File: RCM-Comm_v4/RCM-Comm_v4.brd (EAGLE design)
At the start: 50.8 x 66 mm, 27 parts, among them J1 BLACKFIN_HEADER, J2 2199230-4

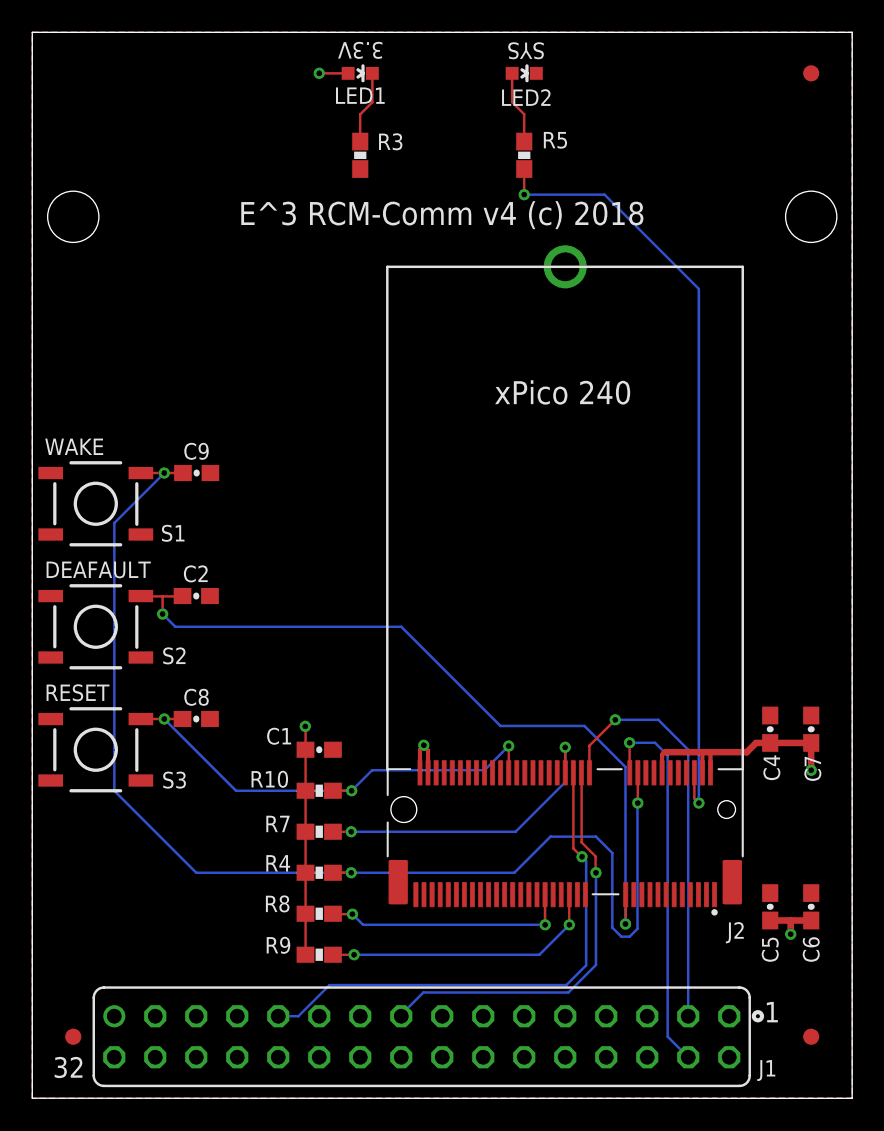
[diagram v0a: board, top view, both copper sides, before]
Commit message: Added DEFAULT ENABLE header back in, re-rendered top and bottom for approval.
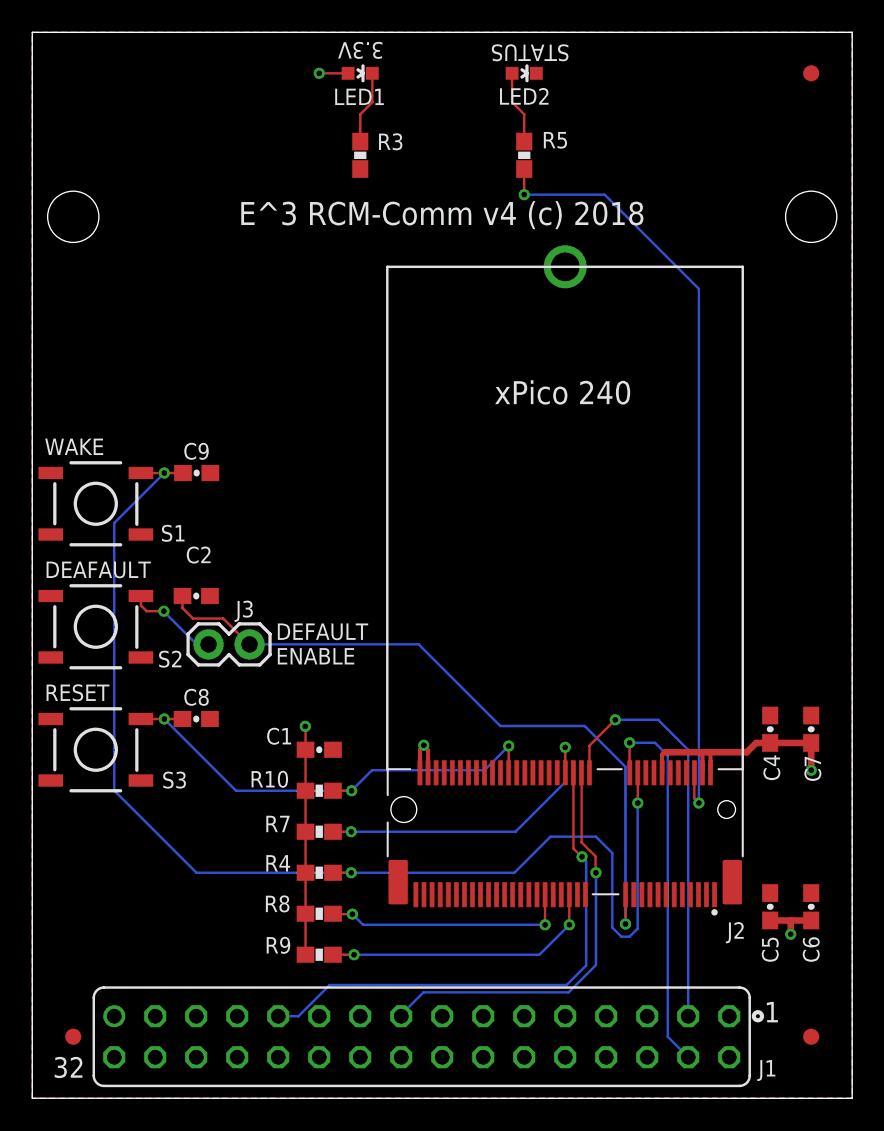
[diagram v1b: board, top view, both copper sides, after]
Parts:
- added J3: (no value), SparkFun-Connectors:1X02
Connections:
- new net N$1: J3.1, S2.3
- net !DEFAULT!: now also J3.2; no longer S2.3
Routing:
- net N$1: track 0.00 -> 5.79 mm, vias 0 -> 1
- net !DEFAULT!: track 47.8 -> 43.9 mm, vias 2 -> 1
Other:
- board text added: "DEFAULT ENABLE"
- board text added: "STATUS"
- board text removed: "SYS"
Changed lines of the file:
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@@
 <layer number="20" name="Dimension" color="15" fill="1" visible="yes" active="yes"/>
 <layer number="21" name="tPlace" color="15" fill="1" visible="yes" active="yes"/>
-<layer number="22" name="bPlace" color="15" fill="1" visible="yes" active="yes"/>
+<layer number="22" name="bPlace" color="15" fill="1" visible="no" active="yes"/>
 <layer number="23" name="tOrigins" color="15" fill="1" visible="yes" active="yes"/>
-<layer number="24" name="bOrigins" color="15" fill="1" visible="yes" active="yes"/>
+<layer number="24" name="bOrigins" color="15" fill="1" visible="no" active="yes"/>
 <layer number="25" name="tNames" color="15" fill="1" visible="yes" active="yes"/>
-<layer number="26" name="bNames" color="15" fill="1" visible="yes" active="yes"/>
+<layer number="26" name="bNames" color="15" fill="1" visible="no" active="yes"/>
 <layer number="27" name="tValues" color="15" fill="1" visible="yes" active="yes"/>
 <layer number="28" name="bValues" color="15" fill="1" visible="yes" active="yes"/>
@@
 <layer number="230" name="230bmp" color="7" fill="1" visible="yes" active="yes"/>
 <layer number="231" name="231bmp" color="7" fill="1" visible="yes" active="yes"/>
+<layer number="232" name="Eagle3D_PG2" color="7" fill="1" visible="yes" active="yes"/>
+<layer number="233" name="Eagle3D_PG3" color="7" fill="1" visible="yes" active="yes"/>
 <layer number="248" name="Housing" color="7" fill="1" visible="yes" active="yes"/>
 <layer number="249" name="Edge" color="7" fill="1" visible="yes" active="yes"/>
@@
 <wire x1="2.54" y1="0" x2="2.54" y2="66.04" width="0" layer="20"/>
 <circle x="47.498" y="5.08" radius="0.254" width="0.254" layer="21"/>
-<text x="15.3162" y="54.102" size="1.4224" layer="21">E^3 RCM-Comm v4 (c) 2018</text>
-<text x="34.3154" y="65.405" size="1.016" layer="21" ratio="10" rot="SR180">SYS</text>
-<text x="24.3332" y="65.4304" size="1.016" layer="21" ratio="10" rot="SR180">3.3V</text>
-<text x="3.302" y="39.8526" size="1.016" layer="21" ratio="10" rot="SR0">WAKE</text>
-<text x="3.302" y="32.2326" size="1.016" layer="21" ratio="10" rot="SR0">DEAFAULT</text>
-<text x="3.302" y="24.6126" size="1.016" layer="21" ratio="10" rot="SR0">RESET</text>
+<text x="15.3162" y="54.102" size="1.4224" layer="21" font="vector">E^3 RCM-Comm v4 (c) 2018</text>
+<text x="35.8394" y="65.278" size="1.016" layer="21" font="vector" ratio="10" rot="SR180">STATUS</text>
+<text x="24.3332" y="65.4304" size="1.016" layer="21" font="vector" ratio="10" rot="SR180">3.3V</text>
+<text x="3.302" y="39.8526" size="1.016" layer="21" font="vector" ratio="10" rot="SR0">WAKE</text>
+<text x="3.302" y="32.2326" size="1.016" layer="21" font="vector" ratio="10" rot="SR0">DEAFAULT</text>
+<text x="3.302" y="24.6126" size="1.016" layer="21" font="vector" ratio="10" rot="SR0">RESET</text>
 <text x="49.0982" y="37.8968" size="1.4224" layer="22" rot="MR0">  Engineering^3, 2018
 http://engineering3.org</text>
@@
 <wire x1="24.5364" y1="20.3708" x2="24.5364" y2="51.5112" width="0.1524" layer="21"/>
 <wire x1="24.5364" y1="51.5112" x2="46.5582" y2="51.5112" width="0.1524" layer="21"/>
-<text x="31.1658" y="43.0022" size="1.4224" layer="21">xPico 240
+<text x="31.1658" y="43.0022" size="1.4224" layer="21" font="vector">xPico 240
 </text>
+<text x="17.6276" y="26.8732" size="1.016" layer="21" font="vector" ratio="10" rot="SR0">DEFAULT
+ENABLE</text>
 </plain>
 <attributes>
@@
 </element>
 <element name="LED1" library="spark_fun" package="LED-0603" value="GREEN" x="22.86" y="63.5" smashed="yes" rot="R270">
-<attribute name="NAME" x="21.2344" y="61.6077" size="1.016" layer="25" font="vector" ratio="12"/>
-<attribute name="VALUE" x="19.5326" y="60.2869" size="1.016" layer="27" font="vector" ratio="12"/>
+<attribute name="NAME" x="21.1836" y="61.5315" size="1.016" layer="25" font="vector" ratio="12"/>
+<attribute name="VALUE" x="20.4724" y="60.2107" size="1.016" layer="27" font="vector" ratio="12"/>
 </element>
 <element name="LED2" library="spark_fun" package="LED-0603" value="GREEN" x="33.02" y="63.5" smashed="yes" rot="R270">
-<attribute name="NAME" x="31.5214" y="61.4807" size="1.016" layer="25" font="vector" ratio="12"/>
-<attribute name="VALUE" x="31.5722" y="60.2107" size="1.016" layer="27" font="vector" ratio="12"/>
+<attribute name="NAME" x="31.3944" y="61.5569" size="1.016" layer="25" font="vector" ratio="12"/>
+<attribute name="VALUE" x="30.8864" y="60.1345" size="1.016" layer="27" font="vector" ratio="12"/>
 </element>
 <element name="R3" library="spark_fun" package="0603-RES" value="330" x="22.86" y="58.42" smashed="yes" rot="R90">
@@
 </element>
 <element name="S2" library="SparkFun-Electromechanical" package="TACTILE-SWITCH-SMD" value="DEFAULTS" x="6.477" y="29.21" smashed="yes" rot="R180">
-<attribute name="NAME" x="10.5664" y="26.8986" size="1.016" layer="25" font="vector" ratio="12"/>
+<attribute name="NAME" x="10.3124" y="26.6954" size="1.016" layer="25" font="vector" ratio="12"/>
 <attribute name="PROD_ID" value="SWCH-08247" x="6.477" y="29.21" size="1.778" layer="27" rot="R180" display="off"/>
 </element>
@@
 </element>
 <element name="C2" library="SparkFun-Capacitors" package="0603-CAP" value="0.1uF" x="12.7" y="31.115" smashed="yes">
-<attribute name="NAME" x="11.8618" y="31.9786" size="1.016" layer="25" font="vector" ratio="12"/>
+<attribute name="NAME" x="12.0396" y="33.147" size="1.016" layer="25" font="vector" ratio="12"/>
 <attribute name="PROD_ID" value="CAP-00810" x="12.7" y="31.115" size="1.778" layer="27" display="off"/>
-<attribute name="VALUE" x="11.2522" y="29.21" size="1.016" layer="27" font="vector" ratio="12"/>
+<attribute name="VALUE" x="11.0236" y="31.9024" size="1.016" layer="27" font="vector" ratio="12"/>
 </element>
 <element name="C8" library="SparkFun-Capacitors" package="0603-CAP" value="0.1uF" x="12.7" y="23.495" smashed="yes">
@@
 <attribute name="NAME" x="16.002" y="19.2532" size="1.016" layer="25" font="vector" ratio="12"/>
 <attribute name="VALUE" x="15.0876" y="17.907" size="1.016" layer="27" font="vector" ratio="12"/>
+</element>
+<element name="J3" library="SparkFun-Connectors" library_urn="urn:adsk.eagle:library:513" package="1X02" package3d_urn="urn:adsk.eagle:package:38039/1" value="" x="13.462" y="28.1178" smashed="yes">
+<attribute name="NAME" x="15.1384" y="29.7942" size="1.016" layer="25" font="vector" ratio="12"/>
+<attribute name="VALUE" x="12.192" y="26.0858" size="0.6096" layer="27" font="vector" ratio="20"/>
 </element>
 </elements>
@@
 </signal>
 <signal name="!DEFAULT!">
-<contactref element="S2" pad="3"/>
 <contactref element="C2" pad="1"/>
 <contactref element="J2" pad="23"/>
@@
 <wire x1="39.2938" y1="20.5232" x2="36.7538" y2="23.0632" width="0.1524" layer="16"/>
 <wire x1="36.7538" y1="23.0632" x2="31.5468" y2="23.0632" width="0.1524" layer="16"/>
-<wire x1="31.5468" y1="23.0632" x2="25.4" y2="29.21" width="0.1524" layer="16"/>
-<wire x1="25.4" y1="29.21" x2="11.4046" y2="29.21" width="0.1524" layer="16"/>
-<wire x1="11.4046" y1="29.21" x2="10.6172" y2="29.9974" width="0.1524" layer="16"/>
-<via x="10.6172" y="29.9974" extent="1-16" drill="0.35"/>
-<wire x1="10.6172" y1="29.9974" x2="10.6172" y2="31.0896" width="0.1524" layer="1"/>
-<wire x1="10.6172" y1="31.0896" x2="11.8246" y2="31.0896" width="0.1524" layer="1"/>
+<wire x1="31.5468" y1="23.0632" x2="26.4922" y2="28.1178" width="0.1524" layer="16"/>
 <wire x1="11.8246" y1="31.0896" x2="11.85" y2="31.115" width="0.1524" layer="1"/>
-<wire x1="10.6172" y1="31.0896" x2="9.2964" y2="31.0896" width="0.1524" layer="1"/>
-<wire x1="9.2964" y1="31.0896" x2="9.271" y2="31.115" width="0.1524" layer="1"/>
+<contactref element="J3" pad="2"/>
+<wire x1="26.4922" y1="28.1178" x2="16.002" y2="28.1178" width="0.1524" layer="16"/>
+<wire x1="11.85" y1="31.115" x2="11.85" y2="30.3648" width="0.1524" layer="1"/>
+<wire x1="11.85" y1="30.3648" x2="12.4968" y2="29.718" width="0.1524" layer="1"/>
+<wire x1="12.4968" y1="29.718" x2="14.3764" y2="29.718" width="0.1524" layer="1"/>
+<wire x1="16.002" y1="28.1178" x2="15.9766" y2="28.1178" width="0.1524" layer="1"/>
+<wire x1="15.9766" y1="28.1178" x2="14.3764" y2="29.718" width="0.1524" layer="1"/>
 </signal>
 <signal name="!EXT_RESET!">
@@
 <wire x1="22.3012" y1="16.51" x2="21.17" y2="16.51" width="0.1524" layer="1"/>
 </signal>
+<signal name="N$1">
+<contactref element="S2" pad="3"/>
+<contactref element="J3" pad="1"/>
+<wire x1="13.462" y1="28.1178" x2="12.7254" y2="28.1178" width="0.1524" layer="16"/>
+<wire x1="12.7254" y1="28.1178" x2="10.6934" y2="30.1498" width="0.1524" layer="16"/>
+<wire x1="10.6934" y1="30.1752" x2="10.6934" y2="30.1498" width="0.1524" layer="16"/>
+<via x="10.6934" y="30.1752" extent="1-16" drill="0.35"/>
+<wire x1="9.271" y1="31.115" x2="9.271" y2="30.5308" width="0.1524" layer="1"/>
+<wire x1="9.271" y1="30.5308" x2="9.6266" y2="30.1752" width="0.1524" layer="1"/>
+<wire x1="9.6266" y1="30.1752" x2="10.6934" y2="30.1752" width="0.1524" layer="1"/>
+</signal>
 </signals>
 <mfgpreviewcolors>
@@
 which will not be processed correctly with this version.
 </note>
+<note version="8.2" severity="warning">
+Since Version 8.2, EAGLE supports online libraries. The ids
+of those online libraries will not be understood (or retained)
+with this version.
+</note>
+<note version="8.3" severity="warning">
+Since Version 8.3, EAGLE supports URNs for individual library
+assets (packages, symbols, and devices). The URNs of those assets
+will not be understood (or retained) with this version.
+</note>
+<note version="8.3" severity="warning">
+Since Version 8.3, EAGLE supports the association of 3D packages
+with devices in libraries, schematics, and board files. Those 3D
+packages will not be understood (or retained) with this version.
+</note>
 </compatibility>
